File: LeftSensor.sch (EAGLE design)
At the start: 9 parts

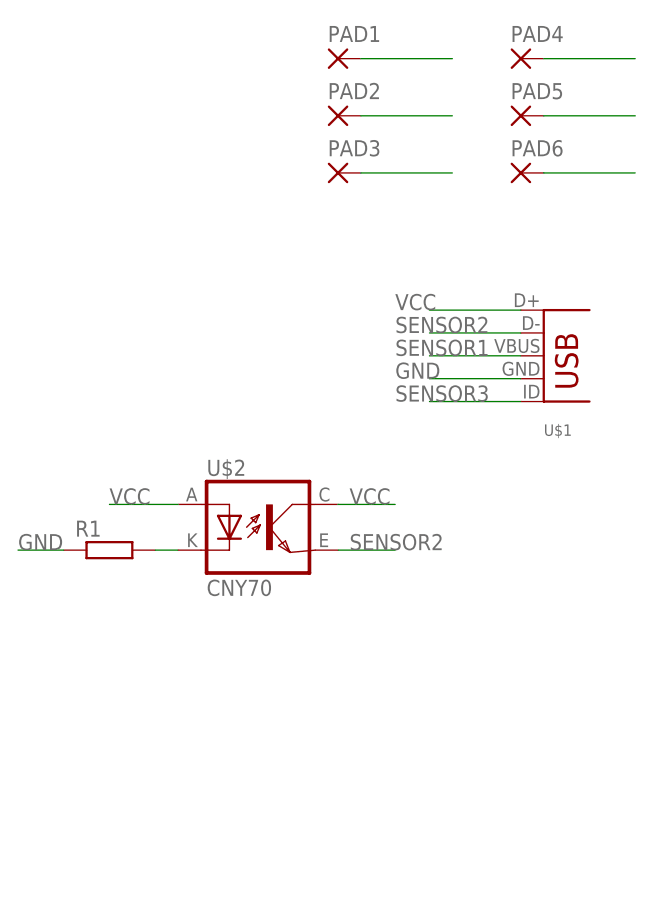
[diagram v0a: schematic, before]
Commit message: Added sensor boards, started on proto frame design
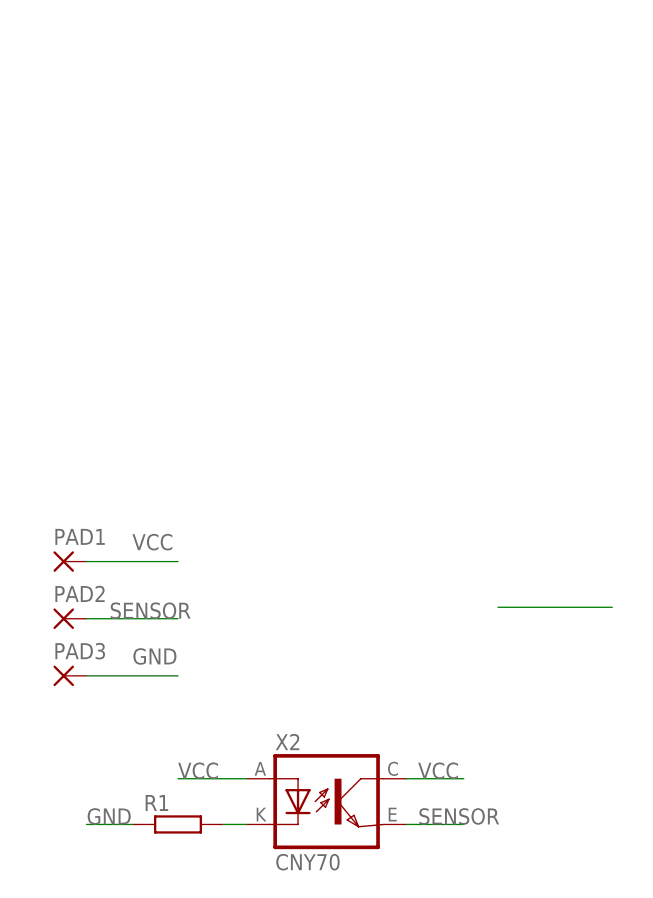
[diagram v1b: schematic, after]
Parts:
- removed PAD4, PAD5, PAD6: WIREPADSMD2,54-5,08, wirepad:WIREPADSMD2,54-5,08
- removed U$1: MOLES-USB-MICRO, tom:MOLES-USB-MICRO
- removed U$2: CNY70, cny70:CNY70
- added X2: CNY70, cny70:CNY70
- PAD1, PAD2, PAD3: value WIREPADSMD2,54-5,08 -> WIREPADSMD1,27-254; device wirepad:WIREPADSMD2,54-5,08 -> wirepad:WIREPADSMD1,27-254
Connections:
- removed net SENSOR1: PAD2.P, U$1.VBUS
- removed net SENSOR2: U$1.D-, U$2.EMI
- removed net SENSOR3: PAD5.P, U$1.ID
- new net SENSOR: PAD2.P, X2.EMI
- net GND: no longer PAD6.P, U$1.GND
- net N$1: now also X2.C; no longer U$2.C
- net VCC: now also X2.A, X2.COL; no longer PAD4.P, U$1.D+, U$2.A, U$2.COL
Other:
- moved on the sheet: PAD1, PAD2, PAD3, R1

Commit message: Added code V1
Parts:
- removed PAD1, PAD2, PAD3: WIREPADSMD1,27-254, wirepad:WIREPADSMD1,27-254
- added PAD4, PAD5, PAD6: WIREPADSMD1,27-254, wirepad:WIREPADSMD1,27-254
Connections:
- net GND: now also PAD6.P; no longer PAD3.P
- net SENSOR: now also PAD5.P; no longer PAD2.P
- net VCC: now also PAD4.P; no longer PAD1.P
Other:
- moved on the sheet: R1, X2
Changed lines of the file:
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@@
 <settings>
 <setting alwaysvectorfont="no"/>
+<setting keepoldvectorfont="yes"/>
 <setting verticaltext="up"/>
 </settings>
@@
 <layer number="88" name="SimResults" color="9" fill="1" visible="yes" active="yes"/>
 <layer number="89" name="SimProbes" color="9" fill="1" visible="yes" active="yes"/>
-<layer number="90" name="Modules" color="5" fill="1" visible="yes" active="yes"/>
+<layer number="90" name="Modules" color="5" fill="1" visible="no" active="yes"/>
 <layer number="91" name="Nets" color="2" fill="1" visible="yes" active="yes"/>
 <layer number="92" name="Busses" color="1" fill="1" visible="yes" active="yes"/>
@@
 <part name="R1" library="ScyllAlarmV3.0" deviceset="RCL_R-EU_" device="R0805"/>
 <part name="X2" library="cny70" deviceset="CNY70" device=""/>
-<part name="PAD1" library="wirepad" library_urn="urn:adsk.eagle:library:412" deviceset="WIREPAD" device="SMD1,27-254" package3d_urn="urn:adsk.eagle:package:30839/1" value="WIREPADSMD1,27-254"/>
-<part name="PAD2" library="wirepad" deviceset="WIREPAD" device="SMD1,27-254" value="WIREPADSMD1,27-254"/>
-<part name="PAD3" library="wirepad" deviceset="WIREPAD" device="SMD1,27-254" value="WIREPADSMD1,27-254"/>
+<part name="PAD4" library="wirepad" deviceset="WIREPAD" device="SMD1,27-254" value="WIREPADSMD1,27-254"/>
+<part name="PAD5" library="wirepad" deviceset="WIREPAD" device="SMD1,27-254" value="WIREPADSMD1,27-254"/>
+<part name="PAD6" library="wirepad" deviceset="WIREPAD" device="SMD1,27-254" value="WIREPADSMD1,27-254"/>
 </parts>
 <sheets>
@@
 </plain>
 <instances>
-<instance part="R1" gate="G$1" x="45.72" y="30.48"/>
-<instance part="X2" gate="G$1" x="63.5" y="33.02"/>
-<instance part="PAD1" gate="G$1" x="33.02" y="59.69" smashed="yes">
-<attribute name="NAME" x="31.877" y="61.5442" size="1.778" layer="95"/>
+<instance part="R1" gate="G$1" x="38.1" y="60.96"/>
+<instance part="X2" gate="G$1" x="55.88" y="63.5"/>
+<instance part="PAD4" gate="G$1" x="45.72" y="90.17" smashed="yes">
+<attribute name="NAME" x="44.577" y="92.0242" size="1.778" layer="95"/>
 </instance>
-<instance part="PAD2" gate="G$1" x="33.02" y="53.34" smashed="yes">
-<attribute name="NAME" x="31.877" y="55.1942" size="1.778" layer="95"/>
+<instance part="PAD5" gate="G$1" x="45.72" y="83.82" smashed="yes">
+<attribute name="NAME" x="44.577" y="85.6742" size="1.778" layer="95"/>
 </instance>
-<instance part="PAD3" gate="G$1" x="33.02" y="46.99" smashed="yes">
-<attribute name="NAME" x="31.877" y="48.8442" size="1.778" layer="95"/>
+<instance part="PAD6" gate="G$1" x="45.72" y="77.47" smashed="yes">
+<attribute name="NAME" x="44.577" y="79.3242" size="1.778" layer="95"/>
 </instance>
 </instances>
@@
 <net name="SENSOR" class="0">
 <segment>
-<pinref part="PAD2" gate="G$1" pin="P"/>
-<wire x1="35.56" y1="53.34" x2="45.72" y2="53.34" width="0.1524" layer="91"/>
-<label x="38.1" y="53.34" size="1.778" layer="95"/>
+<pinref part="PAD5" gate="G$1" pin="P"/>
+<wire x1="48.26" y1="83.82" x2="58.42" y2="83.82" width="0.1524" layer="91"/>
+<label x="50.8" y="83.82" size="1.778" layer="95"/>
 </segment>
 <segment>
 <pinref part="X2" gate="G$1" pin="EMI"/>
-<wire x1="71.12" y1="30.48" x2="77.47" y2="30.48" width="0.1524" layer="91"/>
-<label x="72.39" y="30.48" size="1.778" layer="95"/>
-</segment>
-</net>
-<net name="SENSOR2" class="0">
-<segment>
-<wire x1="93.98" y1="54.61" x2="81.28" y2="54.61" width="0.1524" layer="91"/>
+<wire x1="63.5" y1="60.96" x2="69.85" y2="60.96" width="0.1524" layer="91"/>
+<label x="64.77" y="60.96" size="1.778" layer="95"/>
 </segment>
 </net>
@@
 <segment>
 <pinref part="X2" gate="G$1" pin="A"/>
-<wire x1="53.34" y1="35.56" x2="45.72" y2="35.56" width="0.1524" layer="91"/>
-<label x="45.72" y="35.56" size="1.778" layer="95"/>
+<wire x1="45.72" y1="66.04" x2="38.1" y2="66.04" width="0.1524" layer="91"/>
+<label x="38.1" y="66.04" size="1.778" layer="95"/>
 </segment>
 <segment>
 <pinref part="X2" gate="G$1" pin="COL"/>
-<wire x1="71.12" y1="35.56" x2="77.47" y2="35.56" width="0.1524" layer="91"/>
-<label x="72.39" y="35.56" size="1.778" layer="95"/>
-</segment>
-<segment>
-<pinref part="PAD1" gate="G$1" pin="P"/>
-<wire x1="35.56" y1="59.69" x2="45.72" y2="59.69" width="0.1524" layer="91"/>
-<label x="40.64" y="60.96" size="1.778" layer="95"/>
+<wire x1="63.5" y1="66.04" x2="69.85" y2="66.04" width="0.1524" layer="91"/>
+<label x="64.77" y="66.04" size="1.778" layer="95"/>
+</segment>
+<segment>
+<pinref part="PAD4" gate="G$1" pin="P"/>
+<wire x1="48.26" y1="90.17" x2="58.42" y2="90.17" width="0.1524" layer="91"/>
+<label x="53.34" y="91.44" size="1.778" layer="95"/>
 </segment>
 </net>
@@
 <segment>
 <pinref part="R1" gate="G$1" pin="1"/>
-<wire x1="40.64" y1="30.48" x2="35.56" y2="30.48" width="0.1524" layer="91"/>
-<label x="35.56" y="30.48" size="1.778" layer="95"/>
-</segment>
-<segment>
-<pinref part="PAD3" gate="G$1" pin="P"/>
-<wire x1="35.56" y1="46.99" x2="45.72" y2="46.99" width="0.1524" layer="91"/>
-<label x="40.64" y="48.26" size="1.778" layer="95"/>
+<wire x1="33.02" y1="60.96" x2="27.94" y2="60.96" width="0.1524" layer="91"/>
+<label x="27.94" y="60.96" size="1.778" layer="95"/>
+</segment>
+<segment>
+<pinref part="PAD6" gate="G$1" pin="P"/>
+<wire x1="48.26" y1="77.47" x2="58.42" y2="77.47" width="0.1524" layer="91"/>
+<label x="53.34" y="78.74" size="1.778" layer="95"/>
 </segment>
 </net>
@@
 <pinref part="R1" gate="G$1" pin="2"/>
 <pinref part="X2" gate="G$1" pin="C"/>
-<wire x1="50.8" y1="30.48" x2="53.34" y2="30.48" width="0.1524" layer="91"/>
+<wire x1="43.18" y1="60.96" x2="45.72" y2="60.96" width="0.1524" layer="91"/>
 </segment>
 </net>
@@
 </schematic>
 </drawing>
-<compatibility>
-<note version="8.2" severity="warning">
-Since Version 8.2, EAGLE supports online libraries. The ids
-of those online libraries will not be understood (or retained)
-with this version.
-</note>
-<note version="8.3" severity="warning">
-Since Version 8.3, EAGLE supports URNs for individual library
-assets (packages, symbols, and devices). The URNs of those assets
-will not be understood (or retained) with this version.
-</note>
-<note version="8.3" severity="warning">
-Since Version 8.3, EAGLE supports the association of 3D packages
-with devices in libraries, schematics, and board files. Those 3D
-packages will not be understood (or retained) with this version.
-</note>
-</compatibility>
 </eagle>
